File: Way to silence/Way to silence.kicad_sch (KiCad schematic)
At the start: 5 parts, among them J1 SD Card Connector, U1 ESP32-WROOM-32-N16, U2 SM5308, U4 MAX98357AETE+T

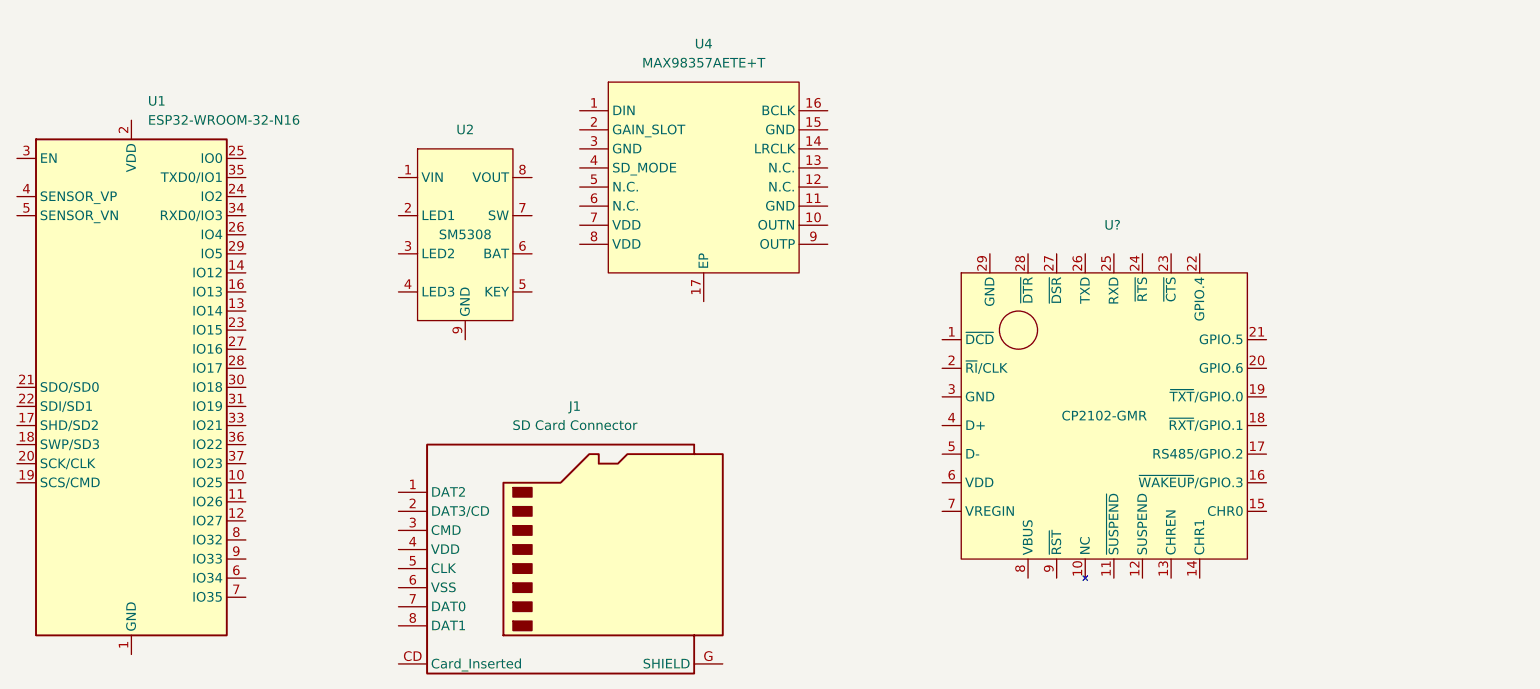
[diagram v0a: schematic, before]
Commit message: [ADD] SD Card Sheet
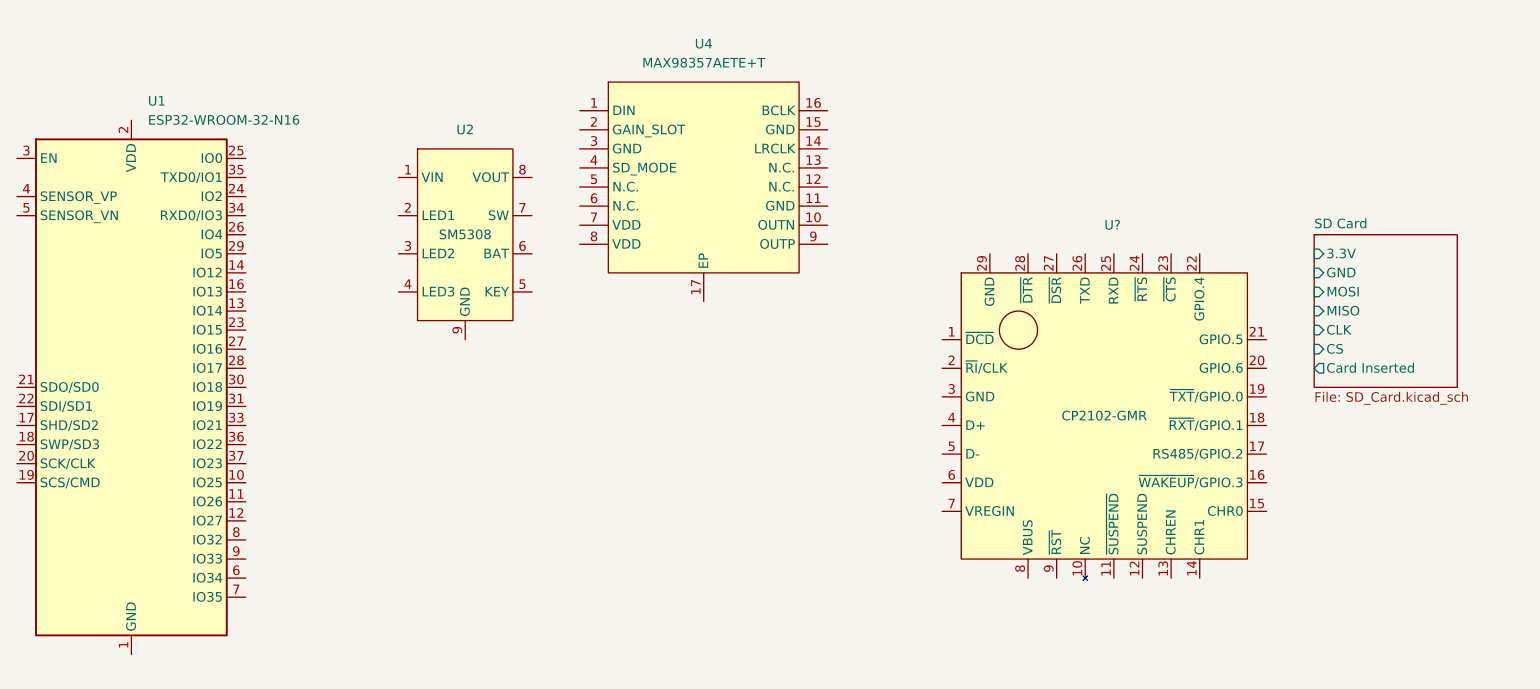
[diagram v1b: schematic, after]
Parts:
- removed J1: SD Card Connector, Way to silence:SD_Card_Connector, symbol Way to silence:SD_Card_Connector
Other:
- added sheet SD Card (SD_Card.kicad_sch)
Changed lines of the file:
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@@
-    )
-  )
-  (symbol (lib_id "Way to silence:SD_Card_Connector") (at 101.6 91.44 0) (unit 1)
-    (in_bom yes) (on_board yes) (dnp no) (fields_autoplaced)
-    (property "Reference" "J1" (at 100.965 71.12 0)
-      (effects (font (size 1.27 1.27)))
-    )
-    (property "Value" "SD Card Connector" (at 100.965 73.66 0)
-      (effects (font (size 1.27 1.27)))
-    )
-    (property "Footprint" "Way to silence:SD_Card_Connector" (at 101.6 60.96 0)
-      (effects (font (size 1.27 1.27)) hide)
-    )
-    (property "Datasheet" "https://datasheet.lcsc.com/lcsc/2209051730_G-Switch-GT-TF003-H0185-02_C5155564.pdf" (at 101.6 64.77 0)
-      (effects (font (size 1.27 1.27)) hide)
-    )
-    (property "LCSC" "C5155564" (at 101.6 72.39 0)
-      (effects (font (size 1.27 1.27)) hide)
-    )
-    (pin "1")
-    (pin "2")
-    (pin "3")
-    (pin "4")
-    (pin "5")
-    (pin "6")
-    (pin "7")
-    (pin "8")
-    (pin "CD")
-    (pin "G")
-    (instances
-      (project "Way to silence"
-        (path "/9822a1be-a034-44c3-8530-56368958b215"
-          (reference "J1") (unit 1)
-        )
-      )
     )
   )
@@
       )
     )
+  )
+  (sheet (at 199.39 48.26) (size 19.05 20.32) (fields_autoplaced)
+    (stroke (width 0.1524) (type solid))
+    (fill (color 0 0 0 0.0000))
+    (property "Sheetname" "SD Card" (at 199.39 47.5484 0)
+      (effects (font (size 1.27 1.27)) (justify left bottom))
+    )
+    (property "Sheetfile" "SD_Card.kicad_sch" (at 199.39 69.1646 0)
+      (effects (font (size 1.27 1.27)) (justify left top))
+    )
+    (pin "MISO" input (at 199.39 58.42 180)
+      (effects (font (size 1.27 1.27)) (justify left))
+    )
+    (pin "3.3V" input (at 199.39 50.8 180)
+      (effects (font (size 1.27 1.27)) (justify left))
+    )
+    (pin "Card Inserted" output (at 199.39 66.04 180)
+      (effects (font (size 1.27 1.27)) (justify left))
+    )
+    (pin "CS" input (at 199.39 63.5 180)
+      (effects (font (size 1.27 1.27)) (justify left))
+    )
+    (pin "CLK" input (at 199.39 60.96 180)
+      (effects (font (size 1.27 1.27)) (justify left))
+    )
+    (pin "MOSI" input (at 199.39 55.88 180)
+      (effects (font (size 1.27 1.27)) (justify left))
+    )
+    (pin "GND" input (at 199.39 53.34 180)
+      (effects (font (size 1.27 1.27)) (justify left))
+    )
+    (instances
+      (project "Way to silence"
+        (path "/9822a1be-a034-44c3-8530-56368958b215" (page "2"))
+      )
+    )

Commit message: [DRC] Working on SD Sheet
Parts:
- gave numbers to parts that had none: 1
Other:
- sheet SD Card ports: added none; removed 3.3V, GND
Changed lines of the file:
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@@
 (kicad_sch (version 20230121) (generator eeschema)
   (paper "A4")
+  (symbol (lib_id "power:PWR_FLAG") (at 177.8 25.4 0) (unit 1)
+    (in_bom yes) (on_board yes) (dnp no) (fields_autoplaced)
+    (property "Reference" "#FLG02" (at 177.8 23.495 0)
+      (effects (font (size 1.27 1.27)) hide)
+    )
+    (property "Value" "PWR_FLAG" (at 177.8 20.32 0)
+      (effects (font (size 1.27 1.27)))
+    )
+    (property "Footprint" "" (at 177.8 25.4 0)
+      (effects (font (size 1.27 1.27)) hide)
+    )
+    (property "Datasheet" "~" (at 177.8 25.4 0)
+      (effects (font (size 1.27 1.27)) hide)
+    )
+    (pin "1")
+    (instances
+      (project "Way to silence"
+        (path "/9822a1be-a034-44c3-8530-56368958b215"
+          (reference "#FLG02") (unit 1)
+        )
+      )
+    )
+  )
   (symbol (lib_id "Way to silence:ESP32-WROOM-32-N16") (at 41.91 68.58 0) (unit 1)
     (in_bom yes) (on_board yes) (dnp no) (fields_autoplaced)
@@
     )
   )
+  (symbol (lib_id "power:+3.3V") (at 177.8 25.4 180) (unit 1)
+    (in_bom yes) (on_board yes) (dnp no) (fields_autoplaced)
+    (property "Reference" "#PWR010" (at 177.8 21.59 0)
+      (effects (font (size 1.27 1.27)) hide)
+    )
+    (property "Value" "+3.3V" (at 177.8 30.48 0)
+      (effects (font (size 1.27 1.27)))
+    )
+    (property "Footprint" "" (at 177.8 25.4 0)
+      (effects (font (size 1.27 1.27)) hide)
+    )
+    (property "Datasheet" "" (at 177.8 25.4 0)
+      (effects (font (size 1.27 1.27)) hide)
+    )
+    (pin "1")
+    (instances
+      (project "Way to silence"
+        (path "/9822a1be-a034-44c3-8530-56368958b215"
+          (reference "#PWR010") (unit 1)
+        )
+      )
+    )
+  )
+  (symbol (lib_id "power:PWR_FLAG") (at 165.1 25.4 0) (unit 1)
+    (in_bom yes) (on_board yes) (dnp no) (fields_autoplaced)
+    (property "Reference" "#FLG01" (at 165.1 23.495 0)
+      (effects (font (size 1.27 1.27)) hide)
+    )
+    (property "Value" "PWR_FLAG" (at 165.1 20.32 0)
+      (effects (font (size 1.27 1.27)))
+    )
+    (property "Footprint" "" (at 165.1 25.4 0)
+      (effects (font (size 1.27 1.27)) hide)
+    )
+    (property "Datasheet" "~" (at 165.1 25.4 0)
+      (effects (font (size 1.27 1.27)) hide)
+    )
+    (pin "1")
+    (instances
+      (project "Way to silence"
+        (path "/9822a1be-a034-44c3-8530-56368958b215"
+          (reference "#FLG01") (unit 1)
+        )
+      )
+    )
+  )
   (symbol (lib_id "Way to silence:MAX98357") (at 118.11 40.64 0) (unit 1)
     (in_bom yes) (on_board yes) (dnp no) (fields_autoplaced)
@@
   (symbol (lib_id "Way to silence:CP2102") (at 171.45 72.39 0) (unit 1)
     (in_bom yes) (on_board yes) (dnp no)
-    (property "Reference" "U?" (at 171.45 46.99 0)
+    (property "Reference" "U3" (at 171.45 46.99 0)
       (effects (font (size 1.27 1.27)) (justify left))
     )
@@
       (project "Way to silence"
         (path "/9822a1be-a034-44c3-8530-56368958b215"
-          (reference "U?") (unit 1)
+          (reference "U3") (unit 1)
+        )
+      )
+    )
+  )
+  (symbol (lib_id "power:GND") (at 165.1 25.4 0) (unit 1)
+    (in_bom yes) (on_board yes) (dnp no) (fields_autoplaced)
+    (property "Reference" "#PWR09" (at 165.1 31.75 0)
+      (effects (font (size 1.27 1.27)) hide)
+    )
+    (property "Value" "GND" (at 165.1 30.48 0)
+      (effects (font (size 1.27 1.27)))
+    )
+    (property "Footprint" "" (at 165.1 25.4 0)
+      (effects (font (size 1.27 1.27)) hide)
+    )
+    (property "Datasheet" "" (at 165.1 25.4 0)
+      (effects (font (size 1.27 1.27)) hide)
+    )
+    (pin "1")
+    (instances
+      (project "Way to silence"
+        (path "/9822a1be-a034-44c3-8530-56368958b215"
+          (reference "#PWR09") (unit 1)
         )
       )
@@
     )
   )
-  (sheet (at 199.39 48.26) (size 19.05 20.32) (fields_autoplaced)
+  (sheet (at 199.39 53.34) (size 19.05 15.24) (fields_autoplaced)
     (stroke (width 0.1524) (type solid))
     (fill (color 0 0 0 0.0000))
-    (property "Sheetname" "SD Card" (at 199.39 47.5484 0)
+    (property "Sheetname" "SD Card" (at 199.39 52.6284 0)
       (effects (font (size 1.27 1.27)) (justify left bottom))
     )
@@
       (effects (font (size 1.27 1.27)) (justify left))
     )
-    (pin "3.3V" input (at 199.39 50.8 180)
-      (effects (font (size 1.27 1.27)) (justify left))
-    )
     (pin "Card Inserted" output (at 199.39 66.04 180)
       (effects (font (size 1.27 1.27)) (justify left))
@@
       (effects (font (size 1.27 1.27)) (justify left))
     )
-    (pin "GND" input (at 199.39 53.34 180)
-      (effects (font (size 1.27 1.27)) (justify left))
-    )

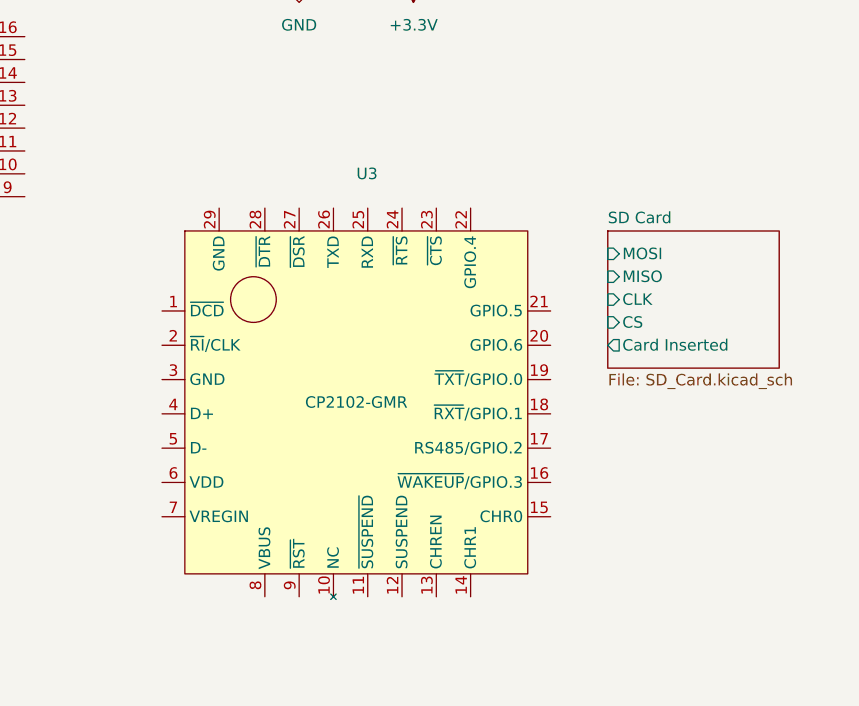
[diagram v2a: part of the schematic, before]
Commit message: [ADD] USB To Uart Sheet
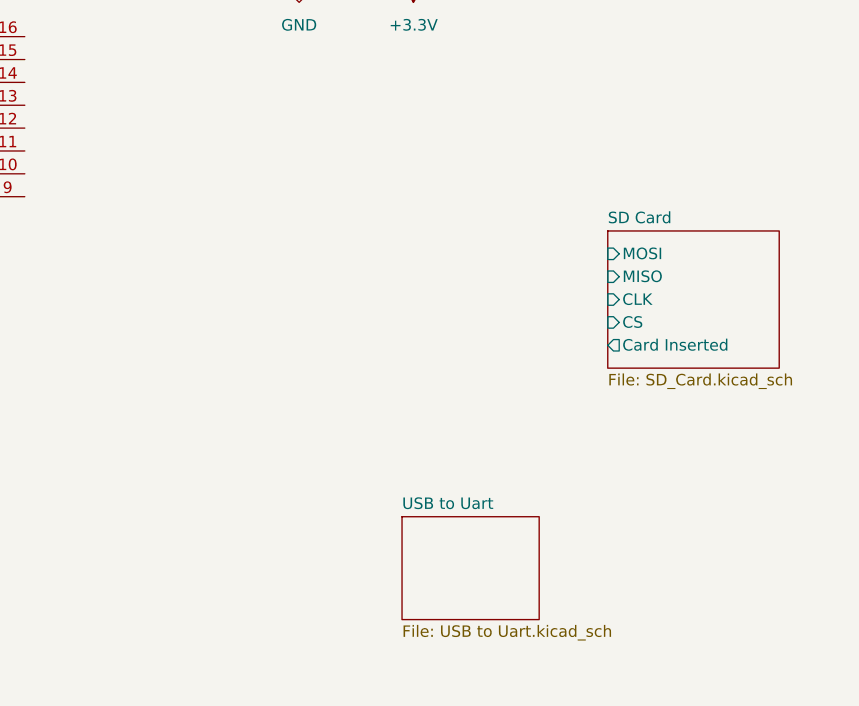
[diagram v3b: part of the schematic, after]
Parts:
- removed U3: CP2102-GMR, Way to silence:CP2102, symbol Way to silence:CP2102
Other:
- added sheet USB to Uart (USB to Uart.kicad_sch)
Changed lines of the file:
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@@
-    )
-  )
-  (symbol (lib_id "Way to silence:CP2102") (at 171.45 72.39 0) (unit 1)
-    (in_bom yes) (on_board yes) (dnp no)
-    (property "Reference" "U3" (at 171.45 46.99 0)
-      (effects (font (size 1.27 1.27)) (justify left))
-    )
-    (property "Value" "CP2102-GMR" (at 171.45 72.39 0)
-      (effects (font (size 1.27 1.27)))
-    )
-    (property "Footprint" "Way to silence:CP2102" (at 171.45 72.39 0)
-      (effects (font (size 1.27 1.27)) hide)
-    )
-    (property "Datasheet" "https://datasheet.lcsc.com/lcsc/1811081920_SILICON-LABS-CP2102-GMR_C6568.pdf" (at 171.45 72.39 0)
-      (effects (font (size 1.27 1.27)) hide)
-    )
-    (property "LCSC" "C6568" (at 171.45 25.4 0)
-      (effects (font (size 1.27 1.27)) hide)
-    )
-    (pin "1")
-    (pin "10")
-    (pin "11")
-    (pin "12")
-    (pin "13")
-    (pin "14")
-    (pin "15")
-    (pin "16")
-    (pin "17")
-    (pin "18")
-    (pin "19")
-    (pin "2")
-    (pin "20")
-    (pin "21")
-    (pin "22")
-    (pin "23")
-    (pin "24")
-    (pin "25")
-    (pin "26")
-    (pin "27")
-    (pin "28")
-    (pin "29")
-    (pin "3")
-    (pin "4")
-    (pin "5")
-    (pin "6")
-    (pin "7")
-    (pin "8")
-    (pin "9")
-    (instances
-      (project "Way to silence"
-        (path "/9822a1be-a034-44c3-8530-56368958b215"
-          (reference "U3") (unit 1)
-        )
-      )
     )
   )
@@
       )
     )
+  )
+  (sheet (at 176.53 85.09) (size 15.24 11.43) (fields_autoplaced)
+    (stroke (width 0.1524) (type solid))
+    (fill (color 0 0 0 0.0000))
+    (property "Sheetname" "USB to Uart" (at 176.53 84.3784 0)
+      (effects (font (size 1.27 1.27)) (justify left bottom))
+    )
+    (property "Sheetfile" "USB to Uart.kicad_sch" (at 176.53 97.1046 0)
+      (effects (font (size 1.27 1.27)) (justify left top))
+    )
+    (instances
+      (project "Way to silence"
+        (path "/9822a1be-a034-44c3-8530-56368958b215" (page "3"))
+      )
+    )

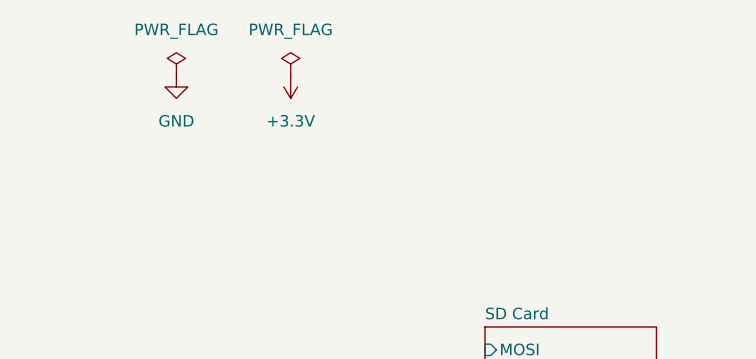
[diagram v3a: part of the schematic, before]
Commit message: [ADD] USB C Connections
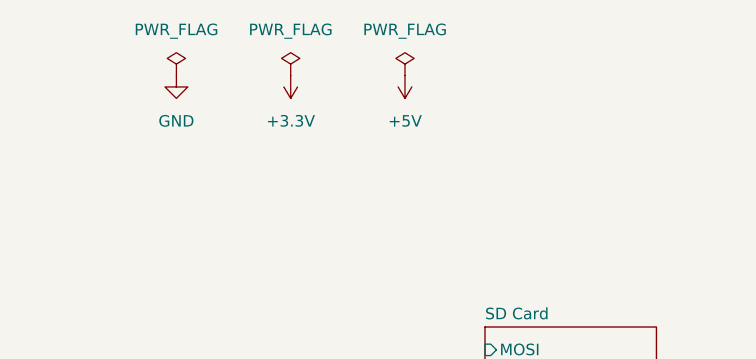
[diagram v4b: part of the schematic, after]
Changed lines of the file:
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@@
+    )
+  )
+  (symbol (lib_id "power:PWR_FLAG") (at 190.5 25.4 0) (unit 1)
+    (in_bom yes) (on_board yes) (dnp no) (fields_autoplaced)
+    (property "Reference" "#FLG03" (at 190.5 23.495 0)
+      (effects (font (size 1.27 1.27)) hide)
+    )
+    (property "Value" "PWR_FLAG" (at 190.5 20.32 0)
+      (effects (font (size 1.27 1.27)))
+    )
+    (property "Footprint" "" (at 190.5 25.4 0)
+      (effects (font (size 1.27 1.27)) hide)
+    )
+    (property "Datasheet" "~" (at 190.5 25.4 0)
+      (effects (font (size 1.27 1.27)) hide)
+    )
+    (pin "1")
+    (instances
+      (project "Way to silence"
+        (path "/9822a1be-a034-44c3-8530-56368958b215"
+          (reference "#FLG03") (unit 1)
+        )
+      )
     )
   )
@@
         )
       )
+    )
+  )
+  (symbol (lib_id "power:+5V") (at 190.5 25.4 180) (unit 1)
+    (in_bom yes) (on_board yes) (dnp no) (fields_autoplaced)
+    (property "Reference" "#PWR04" (at 190.5 21.59 0)
+      (effects (font (size 1.27 1.27)) hide)
+    )
+    (property "Value" "+5V" (at 190.5 30.48 0)
+      (effects (font (size 1.27 1.27)))
+    )
+    (property "Footprint" "" (at 190.5 25.4 0)
+      (effects (font (size 1.27 1.27)) hide)
+    )
+    (property "Datasheet" "" (at 190.5 25.4 0)
+      (effects (font (size 1.27 1.27)) hide)
+    )
+    (pin "1")
+    (instances
+      (project "Way to silence"
+        (path "/9822a1be-a034-44c3-8530-56368958b215"
+          (reference "#PWR04") (unit 1)
+        )
+      )

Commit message: [DRC] Working on USB to UART Sheet
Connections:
- no-connect marks 0 -> 9
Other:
- sheet USB to Uart ports: added EN, IO0, RXD, TXD; removed none
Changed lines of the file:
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@@
 (kicad_sch (version 20230121) (generator eeschema)
   (paper "A4")
+  (no_connect (at 176.53 95.25))
+  (no_connect (at 199.39 60.96))
+  (no_connect (at 199.39 63.5))
+  (no_connect (at 176.53 92.71))
+  (no_connect (at 199.39 55.88))
+  (no_connect (at 176.53 90.17))
+  (no_connect (at 199.39 58.42))
+  (no_connect (at 176.53 87.63))
+  (no_connect (at 199.39 66.04))
   (symbol (lib_id "power:PWR_FLAG") (at 177.8 25.4 0) (unit 1)
     (in_bom yes) (on_board yes) (dnp no) (fields_autoplaced)
@@
       (effects (font (size 1.27 1.27)) (justify left top))
     )
-    (instances
+    (pin "EN" output (at 176.53 87.63 180)
+      (effects (font (size 1.27 1.27)) (justify left))
+    )
+    (pin "IO0" output (at 176.53 90.17 180)
+      (effects (font (size 1.27 1.27)) (justify left))
+    )
+    (pin "TXD" bidirectional (at 176.53 92.71 180)
+      (effects (font (size 1.27 1.27)) (justify left))
+    )
+    (pin "RXD" output (at 176.53 95.25 180)
+      (effects (font (size 1.27 1.27)) (justify left))
+    )
+    (instances
